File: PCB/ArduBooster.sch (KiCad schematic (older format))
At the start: 0 parts

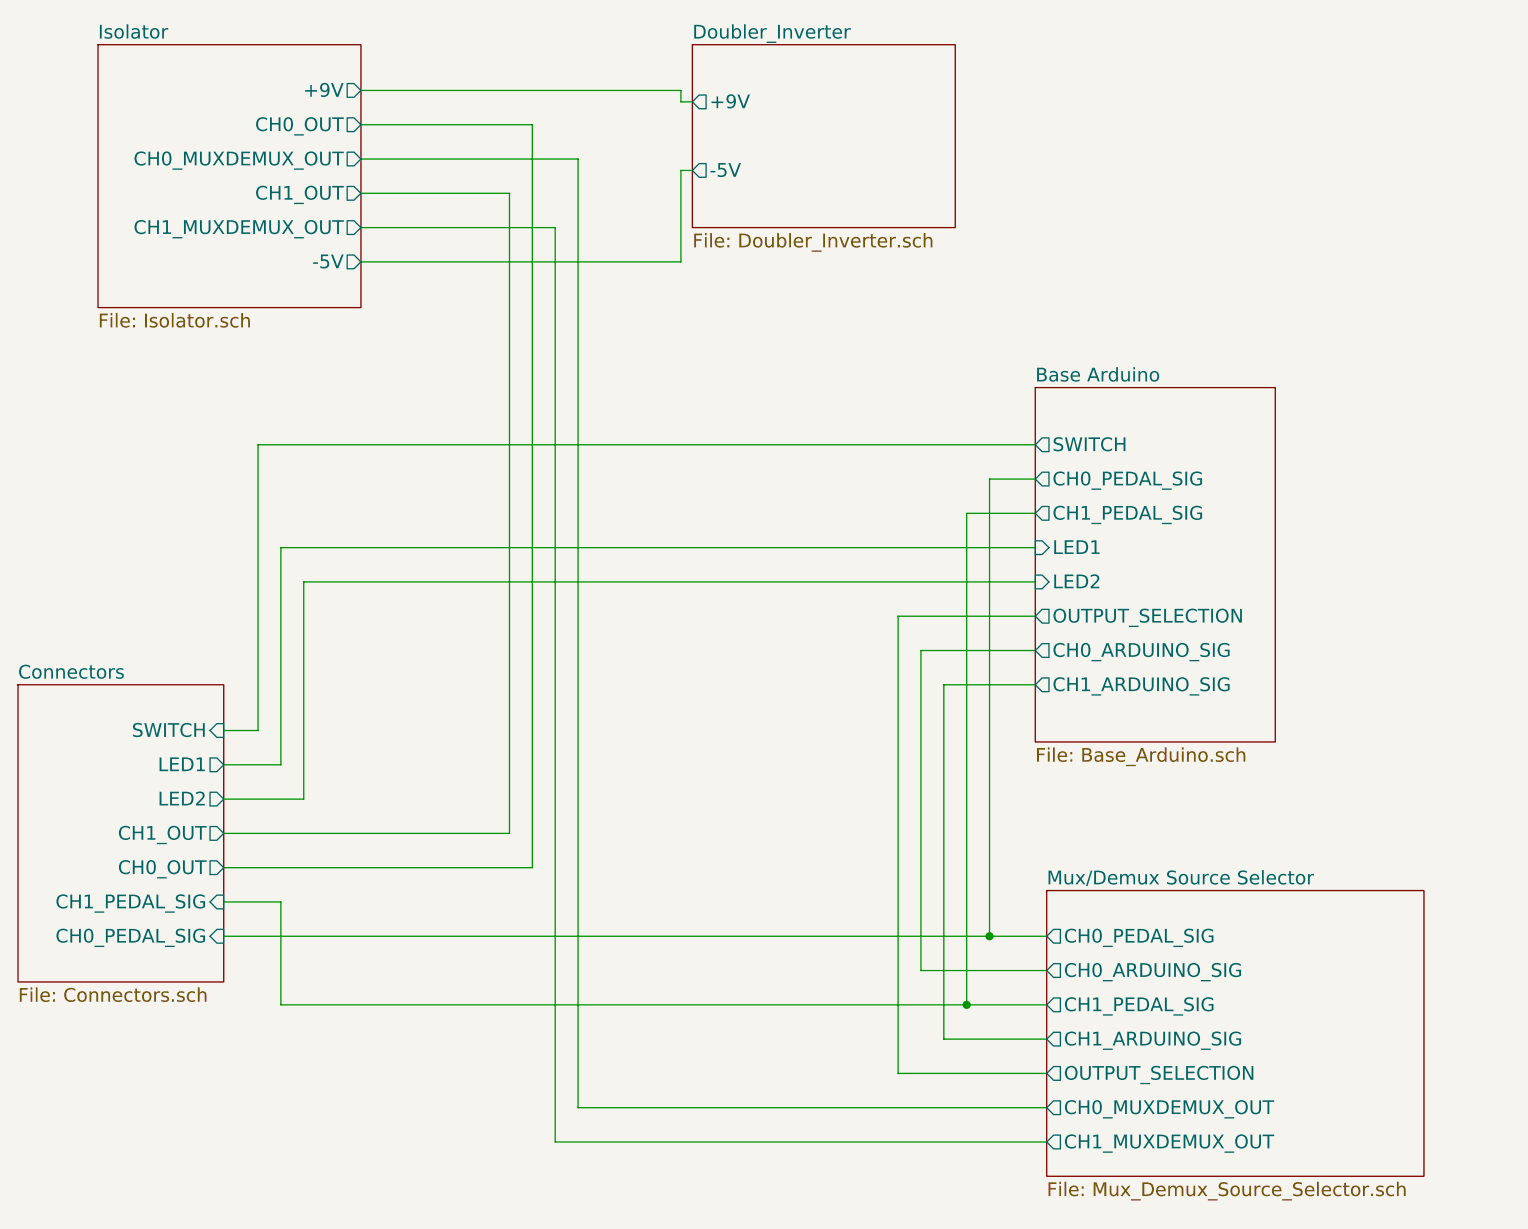
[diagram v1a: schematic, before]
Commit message: New connectors connection. Labels corrections (direction).
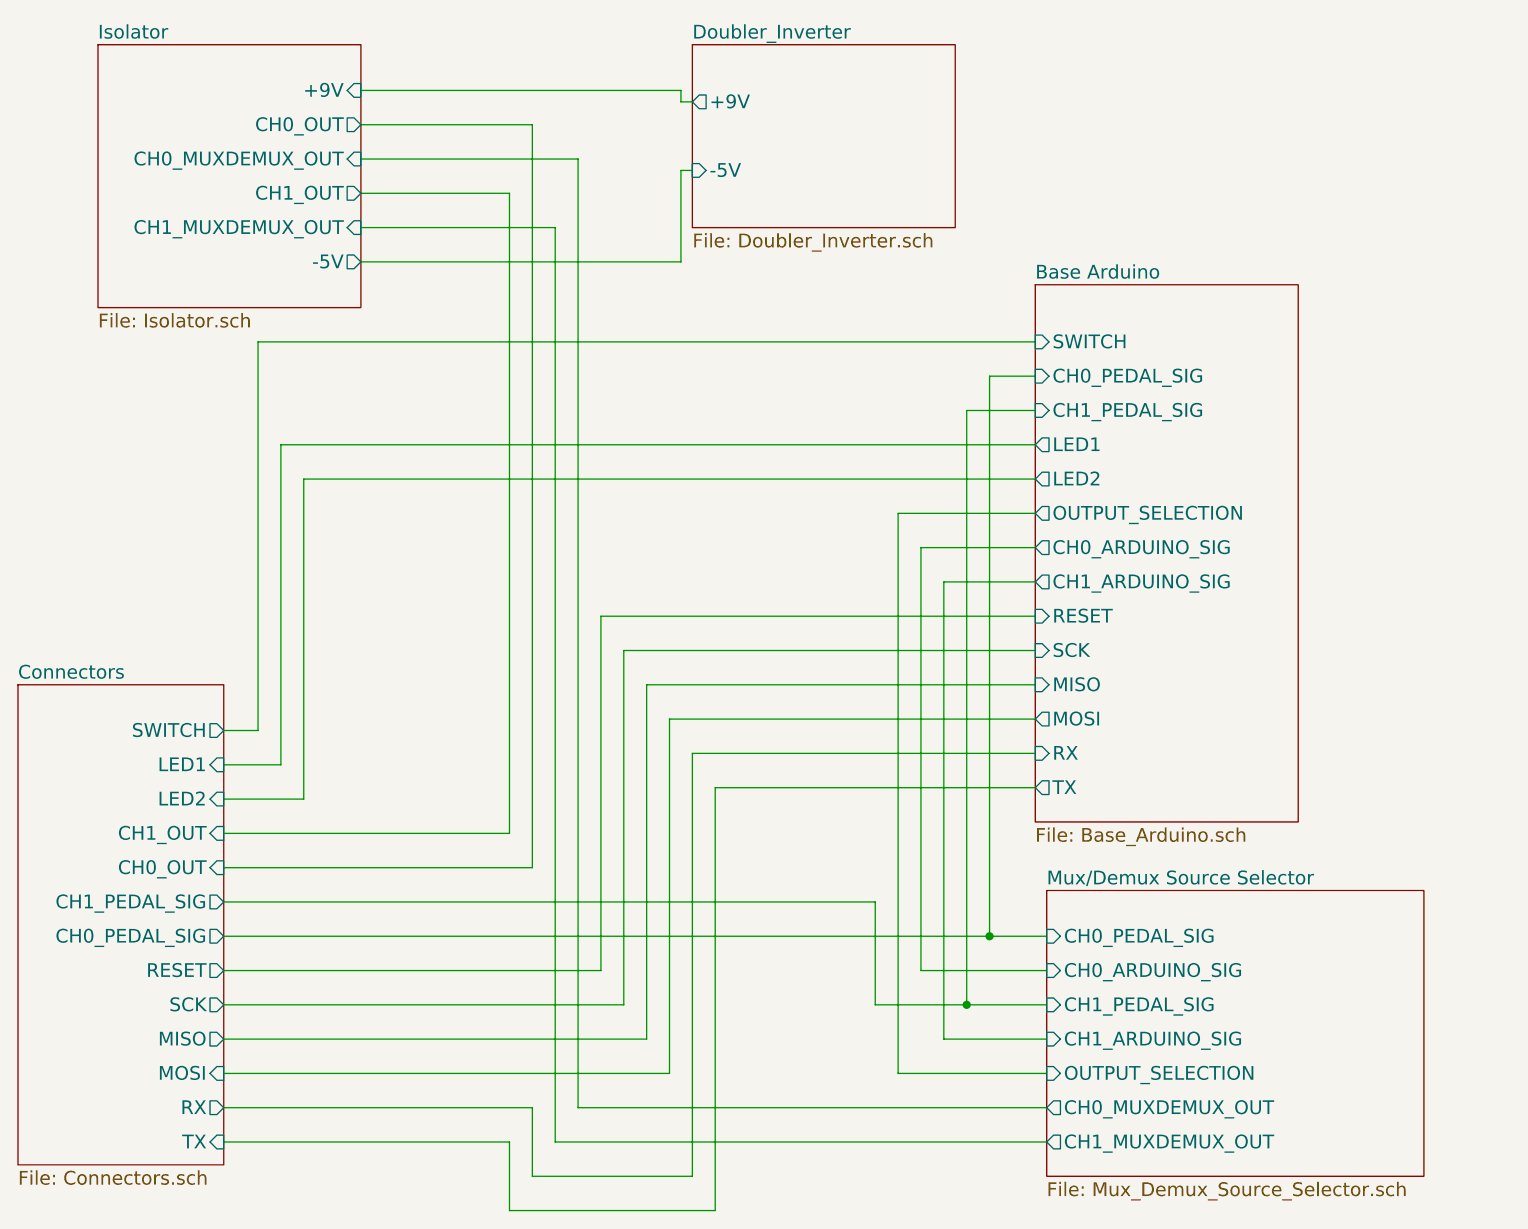
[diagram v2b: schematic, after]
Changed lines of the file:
@@
 $EndDescr
 $Sheet
-S 2850 3700 900  1300
+S 2850 3700 900  2100
 U 54D7C286
 F0 "Connectors" 60
 F1 "Connectors.sch" 60
-F2 "SWITCH" I R 3750 3900 60
-F3 "LED1" O R 3750 4050 60
-F4 "LED2" O R 3750 4200 60
-F5 "CH1_OUT" O R 3750 4350 60
-F6 "CH0_OUT" O R 3750 4500 60
-F7 "CH1_PEDAL_SIG" I R 3750 4650 60
-F8 "CH0_PEDAL_SIG" I R 3750 4800 60
+F2 "SWITCH" O R 3750 3900 60
+F3 "LED1" I R 3750 4050 60
+F4 "LED2" I R 3750 4200 60
+F5 "CH1_OUT" I R 3750 4350 60
+F6 "CH0_OUT" I R 3750 4500 60
+F7 "CH1_PEDAL_SIG" O R 3750 4650 60
+F8 "CH0_PEDAL_SIG" O R 3750 4800 60
+F9 "RESET" O R 3750 4950 60
+F10 "SCK" O R 3750 5100 60
+F11 "MISO" O R 3750 5250 60
+F12 "MOSI" I R 3750 5400 60
+F13 "RX" O R 3750 5550 60
+F14 "TX" I R 3750 5700 60
 $EndSheet
 $Sheet
@@
 F0 "Doubler_Inverter" 60
 F1 "Doubler_Inverter.sch" 60
-F2 "-5V" O L 5800 1450 60
+F2 "-5V" I L 5800 1450 60
 F3 "+9V" O L 5800 1150 60
 $EndSheet
@@
 F0 "Isolator" 60
 F1 "Isolator.sch" 60
-F2 "+9V" O R 4350 1100 60
+F2 "+9V" I R 4350 1100 60
 F3 "CH0_OUT" O R 4350 1250 60
 F4 "-5V" O R 4350 1850 60
-F5 "CH0_MUXDEMUX_OUT" O R 4350 1400 60
-F6 "CH1_MUXDEMUX_OUT" O R 4350 1700 60
+F5 "CH0_MUXDEMUX_OUT" I R 4350 1400 60
+F6 "CH1_MUXDEMUX_OUT" I R 4350 1700 60
 F7 "CH1_OUT" O R 4350 1550 60
 $EndSheet
@@
 F0 "Mux/Demux Source Selector" 60
 F1 "Mux_Demux_Source_Selector.sch" 60
-F2 "CH0_PEDAL_SIG" O L 7350 4800 60
-F3 "CH0_ARDUINO_SIG" O L 7350 4950 60
-F4 "CH1_PEDAL_SIG" O L 7350 5100 60
-F5 "CH1_ARDUINO_SIG" O L 7350 5250 60
-F6 "OUTPUT_SELECTION" O L 7350 5400 60
+F2 "CH0_PEDAL_SIG" I L 7350 4800 60
+F3 "CH0_ARDUINO_SIG" I L 7350 4950 60
+F4 "CH1_PEDAL_SIG" I L 7350 5100 60
+F5 "CH1_ARDUINO_SIG" I L 7350 5250 60
+F6 "OUTPUT_SELECTION" I L 7350 5400 60
 F7 "CH1_MUXDEMUX_OUT" O L 7350 5700 60
 F8 "CH0_MUXDEMUX_OUT" O L 7350 5550 60
 $EndSheet
 $Sheet
-S 7300 2400 1050 1550
+S 7300 1950 1150 2350
 U 54D7EFEF
 F0 "Base Arduino" 60
 F1 "Base_Arduino.sch" 60
-F2 "SWITCH" O L 7300 2650 60
-F3 "CH1_PEDAL_SIG" O L 7300 2950 60
-F4 "CH0_PEDAL_SIG" O L 7300 2800 60
-F5 "LED1" I L 7300 3100 60
-F6 "LED2" I L 7300 3250 60
-F7 "OUTPUT_SELECTION" O L 7300 3400 60
-F8 "CH1_ARDUINO_SIG" O L 7300 3700 60
-F9 "CH0_ARDUINO_SIG" O L 7300 3550 60
+F2 "SWITCH" I L 7300 2200 60
+F3 "CH1_PEDAL_SIG" I L 7300 2500 60
+F4 "CH0_PEDAL_SIG" I L 7300 2350 60
+F5 "LED1" O L 7300 2650 60
+F6 "LED2" O L 7300 2800 60
+F7 "OUTPUT_SELECTION" O L 7300 2950 60
+F8 "CH1_ARDUINO_SIG" O L 7300 3250 60
+F9 "CH0_ARDUINO_SIG" O L 7300 3100 60
+F10 "RESET" I L 7300 3400 60
+F11 "SCK" I L 7300 3550 60
+F12 "MISO" I L 7300 3700 60
+F13 "MOSI" O L 7300 3850 60
+F14 "RX" I L 7300 4000 60
+F15 "TX" O L 7300 4150 60
 $EndSheet
 Wire Wire Line
@@
 	5750 1450 5800 1450
 Wire Wire Line
-	7300 2650 3900 2650
-Wire Wire Line
-	3900 2650 3900 3900
-Wire Wire Line
 	3900 3900 3750 3900
 Wire Wire Line
-	7300 3100 4000 3100
-Wire Wire Line
-	4000 3100 4000 4050
-Wire Wire Line
 	4000 4050 3750 4050
 Wire Wire Line
-	7300 3250 4100 3250
-Wire Wire Line
-	4100 3250 4100 4200
+	4100 2800 4100 4200
 Wire Wire Line
 	4100 4200 3750 4200
@@
 	7350 5400 6700 5400
 Wire Wire Line
-	6700 5400 6700 3400
-Wire Wire Line
-	6700 3400 7300 3400
-Wire Wire Line
-	7300 3550 6800 3550
-Wire Wire Line
-	6800 3550 6800 4950
+	6800 3100 6800 4950
 Wire Wire Line
 	6800 4950 7350 4950
 Wire Wire Line
-	7300 3700 6900 3700
-Wire Wire Line
-	6900 3700 6900 5250
+	6900 3250 6900 5250
 Wire Wire Line
 	6900 5250 7350 5250
 Wire Wire Line
-	7100 2800 7300 2800
-Wire Wire Line
-	4000 5100 7350 5100
-Wire Wire Line
-	7000 5100 7000 2950
-Wire Wire Line
-	7000 2950 7300 2950
-Wire Wire Line
 	4350 1400 5300 1400
 Wire Wire Line
@@
 	5000 4350 3750 4350
 Wire Wire Line
-	7100 4800 7100 2800
-Wire Wire Line
 	3750 4800 7350 4800
+Wire Wire Line
+	3750 4650 6600 4650
+Connection ~ 7000 5100
+Wire Wire Line
+	5400 4950 3750 4950
+Wire Wire Line
+	7300 2200 3900 2200
+Wire Wire Line
+	3900 2200 3900 3900
+Wire Wire Line
+	4000 2650 7300 2650
+Wire Wire Line
+	4000 2650 4000 4050
+Wire Wire Line
+	4100 2800 7300 2800
+Wire Wire Line
+	7300 3400 5400 3400
+Wire Wire Line
+	5400 3400 5400 4950
+Wire Wire Line
+	7300 2500 7000 2500
+Wire Wire Line
+	7000 2500 7000 5100
+Wire Wire Line
+	7100 4800 7100 2350
+Wire Wire Line
+	7100 2350 7300 2350
 Connection ~ 7100 4800
 Wire Wire Line
-	4000 5100 4000 4650
-Wire Wire Line
-	4000 4650 3750 4650
-Connection ~ 7000 5100
+	7300 2950 6700 2950
+Wire Wire Line
+	6700 2950 6700 5400
+Wire Wire Line
+	7300 3100 6800 3100
+Wire Wire Line
+	7300 3250 6900 3250
+Wire Wire Line
+	6600 4650 6600 5100
+Wire Wire Line
+	6600 5100 7350 5100
+Wire Wire Line
+	3750 5100 5500 5100
+Wire Wire Line
+	5500 5100 5500 3550
+Wire Wire Line
+	5500 3550 7300 3550
+Wire Wire Line
+	3750 5250 5600 5250
+Wire Wire Line
+	5600 5250 5600 3700
+Wire Wire Line
+	5600 3700 7300 3700
+Wire Wire Line
+	3750 5400 5700 5400
+Wire Wire Line
+	5700 5400 5700 3850
+Wire Wire Line
+	5700 3850 7300 3850
+Wire Wire Line
+	3750 5550 5100 5550
+Wire Wire Line
+	5100 5550 5100 5850
+Wire Wire Line
+	5100 5850 5800 5850
+Wire Wire Line
+	5800 5850 5800 4000
+Wire Wire Line
+	5800 4000 7300 4000
+Wire Wire Line
+	3750 5700 5000 5700
+Wire Wire Line
+	5000 5700 5000 6000
+Wire Wire Line
+	5000 6000 5900 6000
+Wire Wire Line
+	5900 6000 5900 4150
+Wire Wire Line
+	5900 4150 7300 4150
 $EndSCHEMATC

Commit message: Initial output feedback connection  correction.
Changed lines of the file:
@@
 F8 "CH0_MUXDEMUX_OUT" O L 7350 5550 60
-$EndSheet
-$Sheet
-S 7300 1950 1150 2350
-U 54D7EFEF
-F0 "Base Arduino" 60
-F1 "Base_Arduino.sch" 60
-F2 "SWITCH" I L 7300 2200 60
-F3 "CH1_PEDAL_SIG" I L 7300 2500 60
-F4 "CH0_PEDAL_SIG" I L 7300 2350 60
-F5 "LED1" O L 7300 2650 60
-F6 "LED2" O L 7300 2800 60
-F7 "OUTPUT_SELECTION" O L 7300 2950 60
-F8 "CH1_ARDUINO_SIG" O L 7300 3250 60
-F9 "CH0_ARDUINO_SIG" O L 7300 3100 60
-F10 "RESET" I L 7300 3400 60
-F11 "SCK" I L 7300 3550 60
-F12 "MISO" I L 7300 3700 60
-F13 "MOSI" O L 7300 3850 60
-F14 "RX" I L 7300 4000 60
-F15 "TX" O L 7300 4150 60
 $EndSheet
 Wire Wire Line
@@
 Wire Wire Line
 	5900 4150 7300 4150
+$Sheet
+S 7300 1650 1150 2650
+U 54D7EFEF
+F0 "Base Arduino" 60
+F1 "Base_Arduino.sch" 60
+F2 "SWITCH" I L 7300 2200 60
+F3 "CH1_PEDAL_SIG" I L 7300 2500 60
+F4 "CH0_PEDAL_SIG" I L 7300 2350 60
+F5 "LED1" O L 7300 2650 60
+F6 "LED2" O L 7300 2800 60
+F7 "OUTPUT_SELECTION" O L 7300 2950 60
+F8 "CH1_ARDUINO_SIG" O L 7300 3250 60
+F9 "CH0_ARDUINO_SIG" O L 7300 3100 60
+F10 "RESET" I L 7300 3400 60
+F11 "SCK" I L 7300 3550 60
+F12 "MISO" I L 7300 3700 60
+F13 "MOSI" O L 7300 3850 60
+F14 "RX" I L 7300 4000 60
+F15 "TX" O L 7300 4150 60
+F16 "CH1_OUT" I L 7300 2050 60
+F17 "CH0_OUT" I L 7300 1900 60
+$EndSheet
+Connection ~ 5000 2050
+Connection ~ 5100 1900
+Wire Wire Line
+	5100 1900 7300 1900
+Wire Wire Line
+	7300 2050 5000 2050
 $EndSCHEMATC
